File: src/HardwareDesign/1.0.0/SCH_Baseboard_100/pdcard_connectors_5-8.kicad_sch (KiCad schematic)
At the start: 12 parts, among them J4 10018784-10200TLF

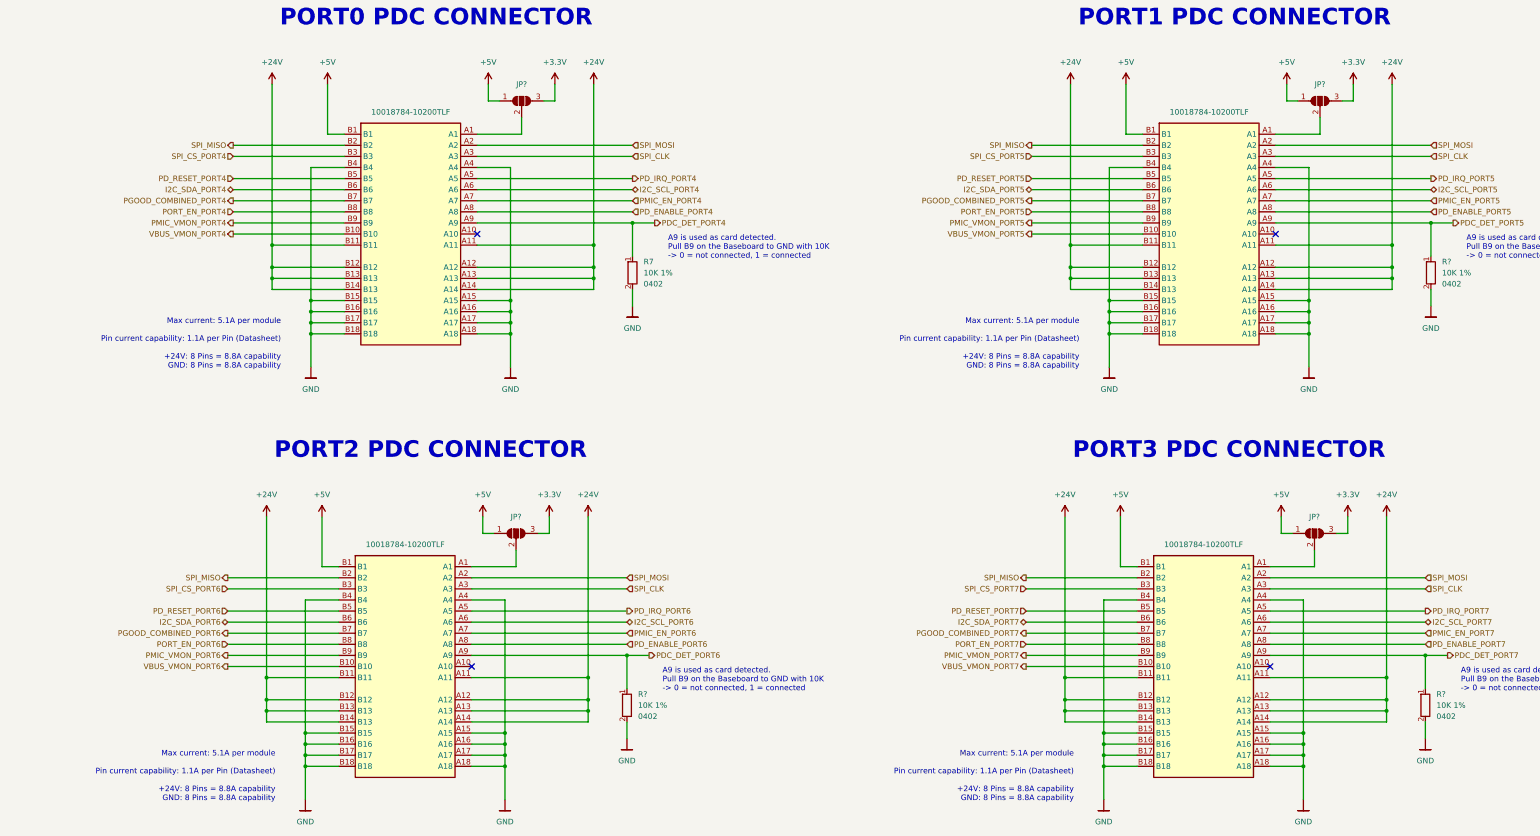
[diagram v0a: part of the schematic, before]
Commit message: Add bladecore to design
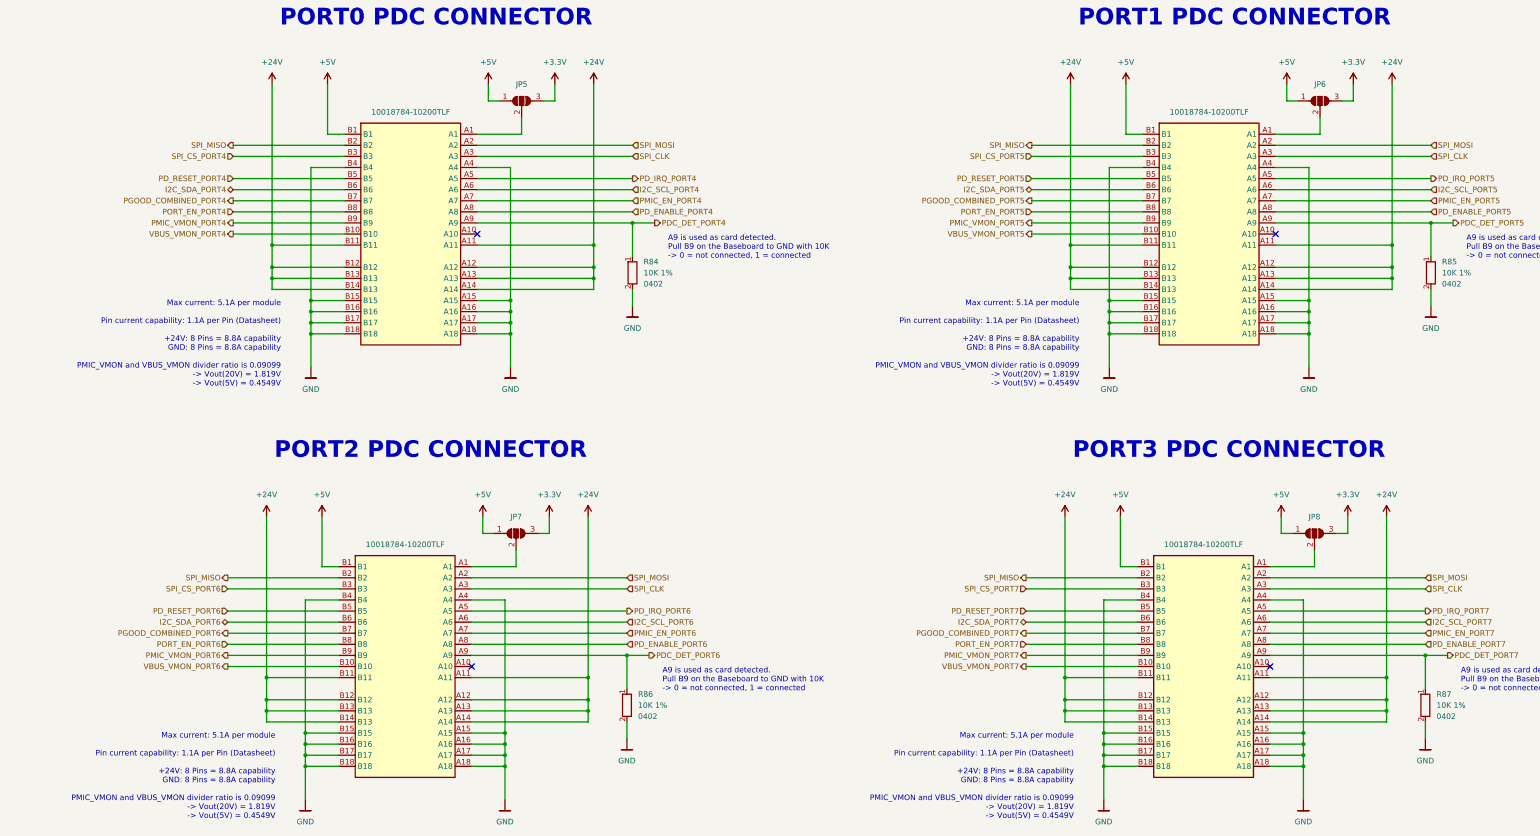
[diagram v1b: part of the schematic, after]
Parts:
- gave numbers to parts that had none: 10
- renumbered J4 to J8, R7 to R84
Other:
- note added: "Max current: 5.1A per module Pin current capability: 1.1A per Pin (Datasheet) +24V: 8 Pins = 8.8A capability GND: 8 Pins = 8.8A capability PMIC_VMON and VBUS_VMON divider ratio is 0.09099 -> Vout(20V) = 1.819V -> Vout(5V) = 0.4549V"
- note removed: "Max current: 5.1A per module Pin current capability: 1.1A per Pin (Datasheet) +24V: 8 Pins = 8.8A capability GND: 8 Pins = 8.8A capability"
